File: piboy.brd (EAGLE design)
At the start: 76.2 x 76.2 mm, 78 parts, among them CN4 MicroUSB, T1 MMUN2133LT1G, U1 TPS61090RSAR, U2 MCP73871

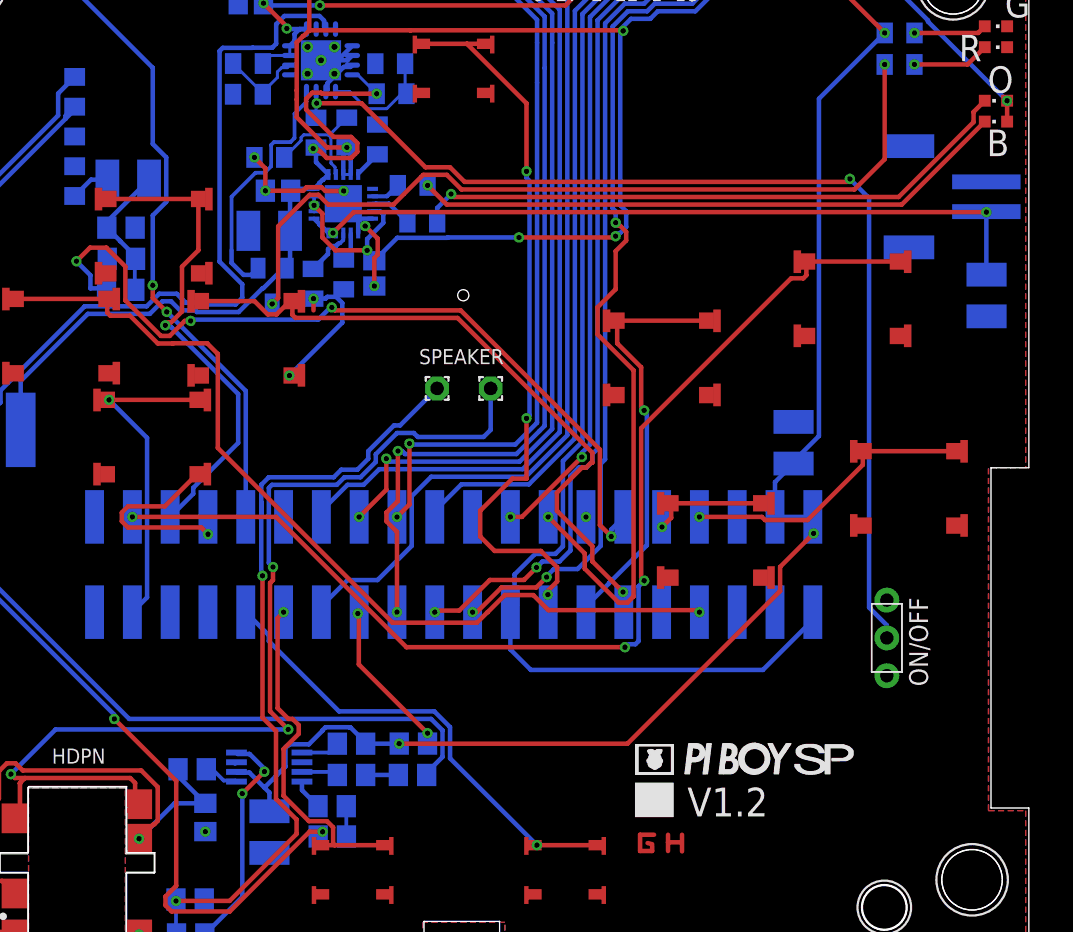
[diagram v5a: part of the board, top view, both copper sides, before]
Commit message: -added safe shutdown circuit
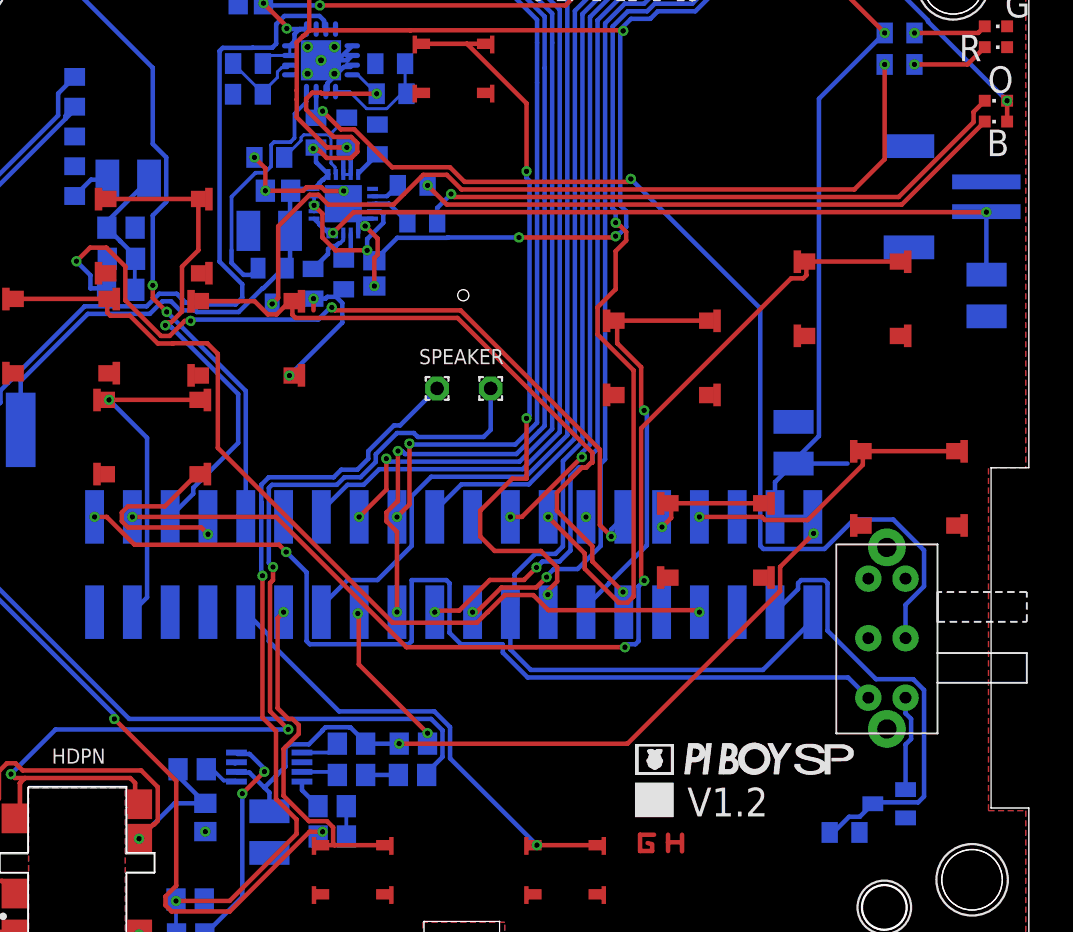
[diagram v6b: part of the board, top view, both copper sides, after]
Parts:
- removed ON/OFF: (no value), piboy_new:ADAFRUIT_EG1218
- added R10: 100K, adafruit:R0805
- added U$31: EG2210-SW, piboy_new:EG2210-SW
- added U$40: MMBF5460, piboy_new:SOT23
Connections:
- new net KEEPALIVE: R10.2, U$40.3, U$9.P3
- new net N$20: U$31.P$3
- new net N$21: U$31.P$1, U$40.1
- new net SHUTDOWN: U$31.P$4, U$9.P40
- net +3.3V: now also U$31.P$5
- net ENABLE: now also U$31.P$2; no longer ON/OFF.P
- net GND: now also R10.1, U$31.P$7, U$31.P$8, U$40.2; no longer ON/OFF.O
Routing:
- net SHUTDOWN: track 0.00 -> 68.0 mm, vias 0 -> 2
- net KEEPALIVE: track 0.00 -> 30.6 mm
- net N$21: track 0.00 -> 6.49 mm
- net +5V: track 144.0 -> 147.6 mm
- net ENABLE: track 72.2 -> 73.2 mm
